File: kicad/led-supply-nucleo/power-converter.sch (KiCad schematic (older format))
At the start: 77 parts, among them J1 Conn_01x03_Female, P1 Conn_WallPlug_Earth, Q1 BC848, Q2 BC848, Q3 IRLZ44N, Q4 IRLZ44N, Q5 IRLZ44N, Q6 IRLZ44N, Q7 IRLZ44N, Q8 IRLZ44N, T1 Transformer_1P_1S, U1 UCC27714D, U2 UCC27714D, U3 UCC27714D

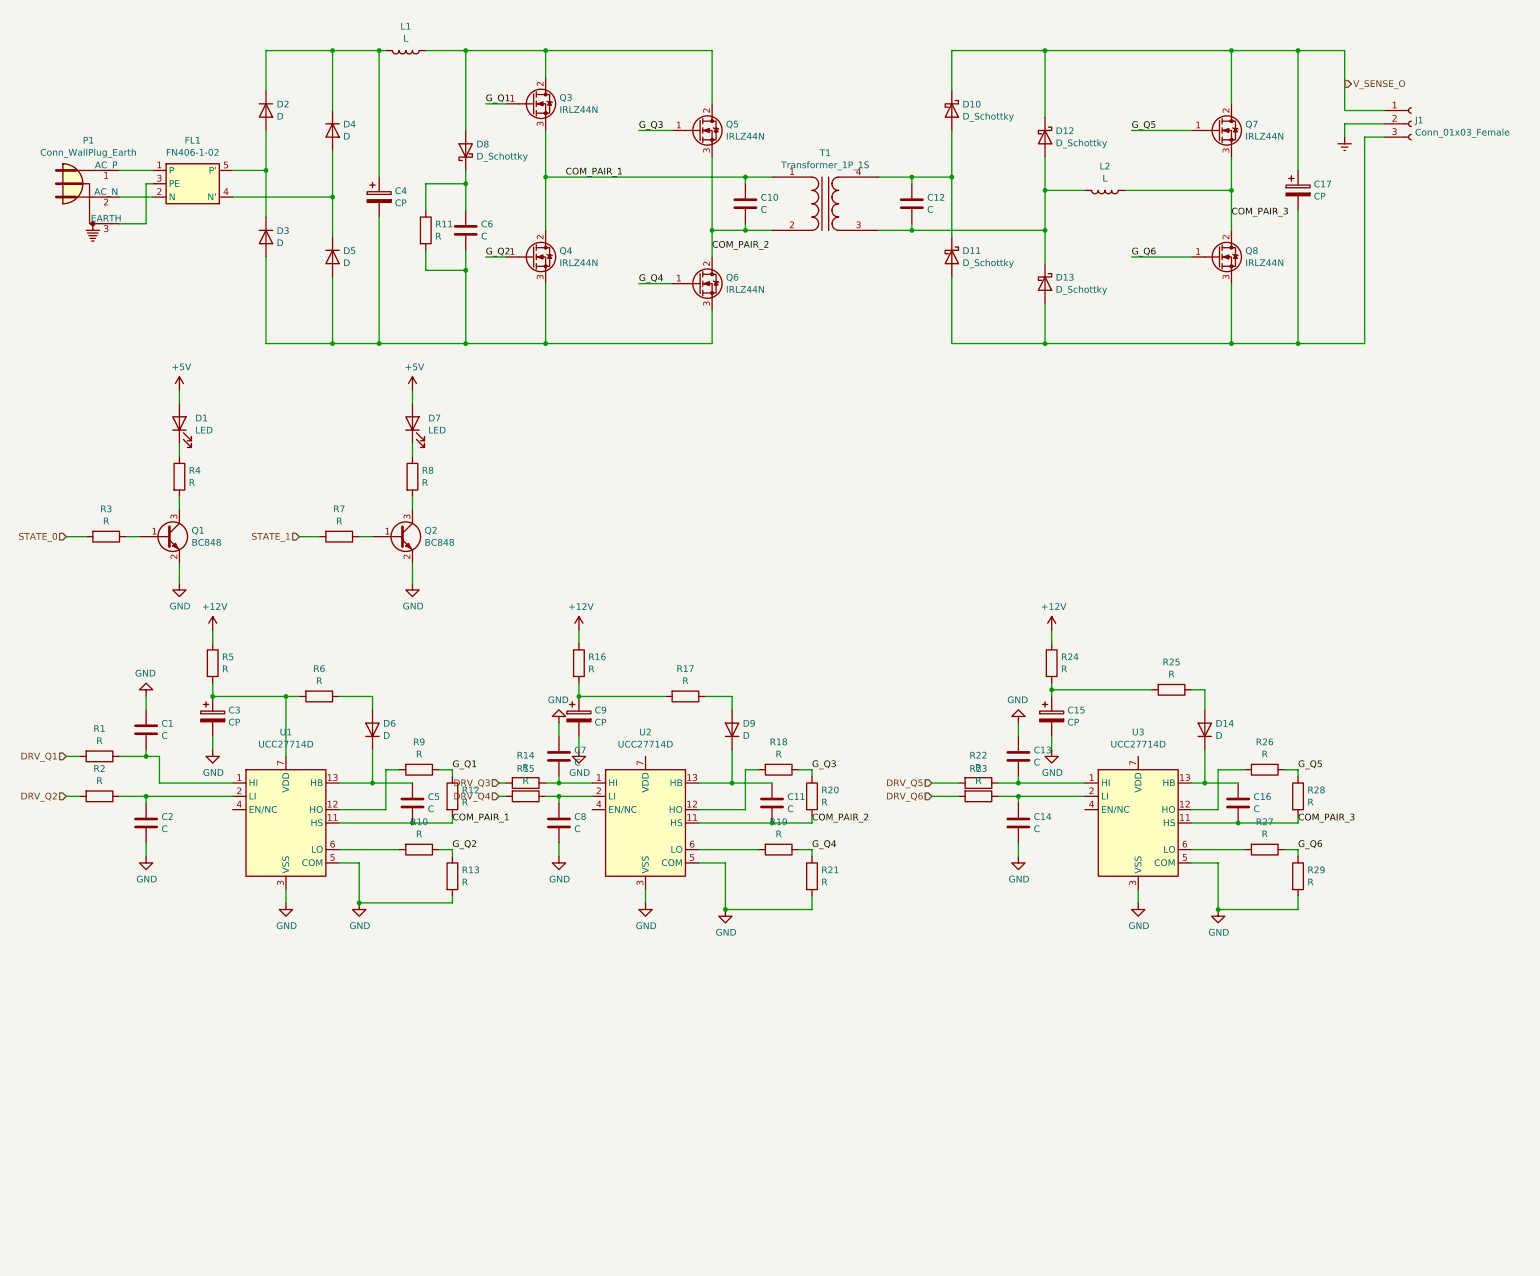
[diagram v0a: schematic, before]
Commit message: Add Nucleo based board for prototyping.
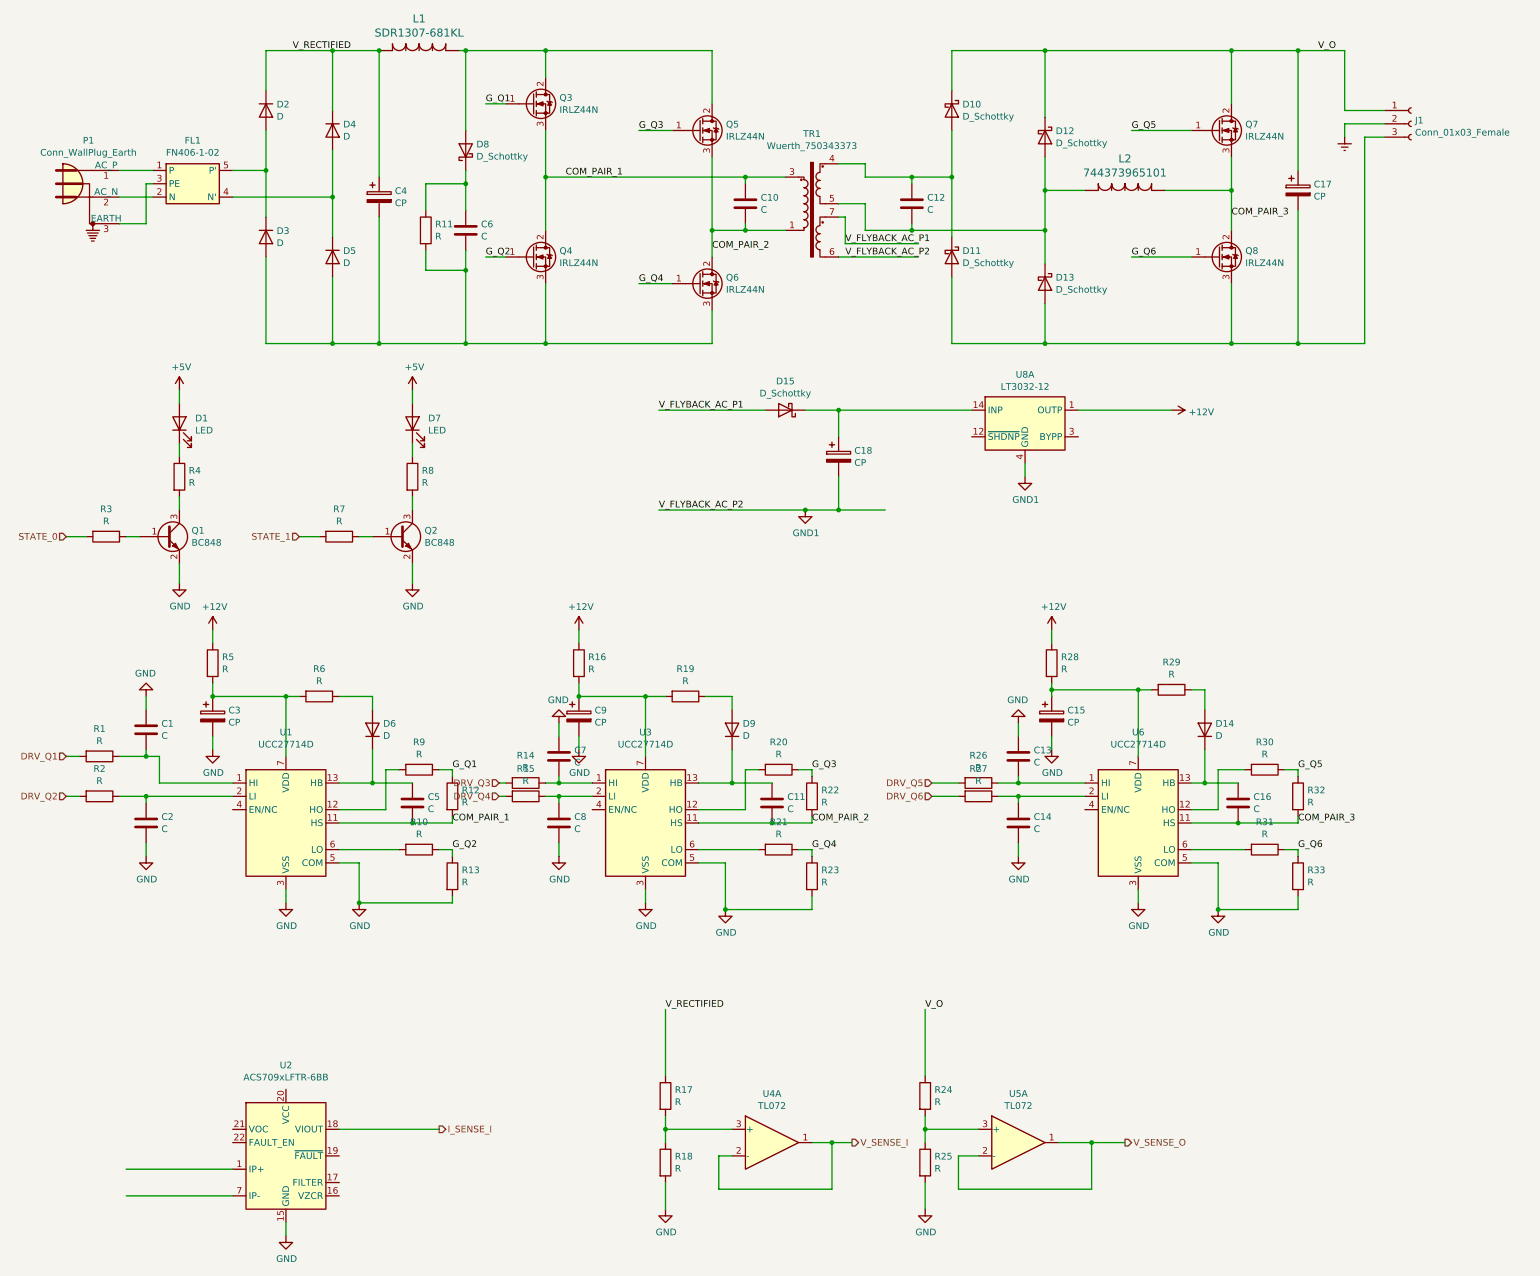
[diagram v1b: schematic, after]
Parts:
- removed L1, L2: L, Inductor_THT:L_Radial_D24.4mm_P22.90mm_muRATA_1400series, symbol Device:L
- removed T1: Transformer_1P_1S, symbol Device:Transformer_1P_1S
- added C18: CP, Capacitor_SMD:CP_Elec_10x12.5, symbol Device:CP
- added D15: D_Schottky, Diode_SMD:D_1210_3225Metric_Pad1.42x2.65mm_HandSolder, symbol Device:D_Schottky
- added L1: SDR1307-681KL, kicad-footprint:SDR1307-681KL, symbol kicad-symbols-SDR1307-681KL:SDR1307-681KL
- added L2: 744373965101, kicad-footprint:744373965101, symbol kicad-symbols-WUERTH-100UH:744373965101
- added R17, R18, R24, R25: R, Resistor_SMD:R_0805_2012Metric_Pad1.20x1.40mm_HandSolder, symbol Device:R
- added TR1: Wuerth_750343373, Transformer_THT:Transformer_Wuerth_750343373, symbol Transformer:Wuerth_750343373
- added U2: ACS709xLFTR-6BB, Sensor_Current:Allegro_QSOP-24_3.9x8.7mm_P0.635mm, symbol Sensor_Current:ACS709xLFTR-6BB
- added U4, U5: TL072, Package_SO:SSOP-14_5.3x6.2mm_P0.65mm, symbol Amplifier_Operational:TL072
- added U8: LT3032-12, Package_DFN_QFN:Linear_DE14MA, symbol Regulator_Linear:LT3032-12
- Q3, Q4, Q5, Q6: footprint Package_TO_SOT_SMD:SOT-223 -> Package_TO_SOT_SMD:SOT-223-3_TabPin2
- renumbered R17 to R19, R18 to R20, R19 to R21, R20 to R22, R21 to R23, R22 to R26, R23 to R27, R24 to R28, R25 to R29, R26 to R30, R27 to R31, R28 to R32, R29 to R33, U2 to U3, U3 to U6
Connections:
- net +12V: now also U8.1 (OUTP)
- net COM_PAIR_1: now also TR1.3
- net COM_PAIR_2: now also TR1.1
- net COM_PAIR_3: now also L2.1
- net GND: now also R18.2, R25.2, U2.15 (GND)
- net V_SENSE_O: now also U5.1, U5.2 (-); no longer C17.1, D10.1 (K), D12.1 (K), J1.1 (Pin_1), Q7.2 (D)
- net V_RECTIFIED: now reaches C4.1, D2.1 (K), D4.1 (K)
- net V_RECTIFIED: now also L1.2, R17.1
- net at U3.7 (VDD): now also C9.1, R16.2, R19.2
- net at U6.7 (VDD): now also C15.1, R28.2, R29.2
- net at D8.2 (A), Q3.2 (D), Q5.2 (D): now also L1.1
- net at C12.2, D12.2 (A), D13.1 (K): now also L2.2, TR1.5
- net at C12.1, D10.2 (A), D11.1 (K): now also TR1.4
- new net: U2.1 (IP+), U2.2 (IP+), U2.3 (IP+), U2.4 (IP+), U2.5 (IP+), U2.6 (IP+)
- new net: U2.10 (IP-), U2.11 (IP-), U2.12 (IP-), U2.7 (IP-), U2.8 (IP-), U2.9 (IP-)
- new net: R17.2, R18.1, U4.3 (+)
- new net: R24.2, R25.1, U5.3 (+)
- new net: C18.1, D15.1 (K), U8.14 (INP)
- new net GND1: C18.2, TR1.6, U8.4 (GND)
- new net I_SENSE_I: U2.18 (VIOUT)
- new net V_FLYBACK_AC_P1: D15.2 (A), TR1.7
- new net V_O: C17.1, D10.1 (K), D12.1 (K), J1.1 (Pin_1), Q7.2 (D), R24.1
- new net V_SENSE_I: U4.1, U4.2 (-)
